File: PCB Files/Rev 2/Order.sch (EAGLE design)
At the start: 188 parts, among them IC1 ATMEGA32A-PU, J1 USB4085-GF-A_REVA, SW1 EC12E_SW, X1 49S/18PF

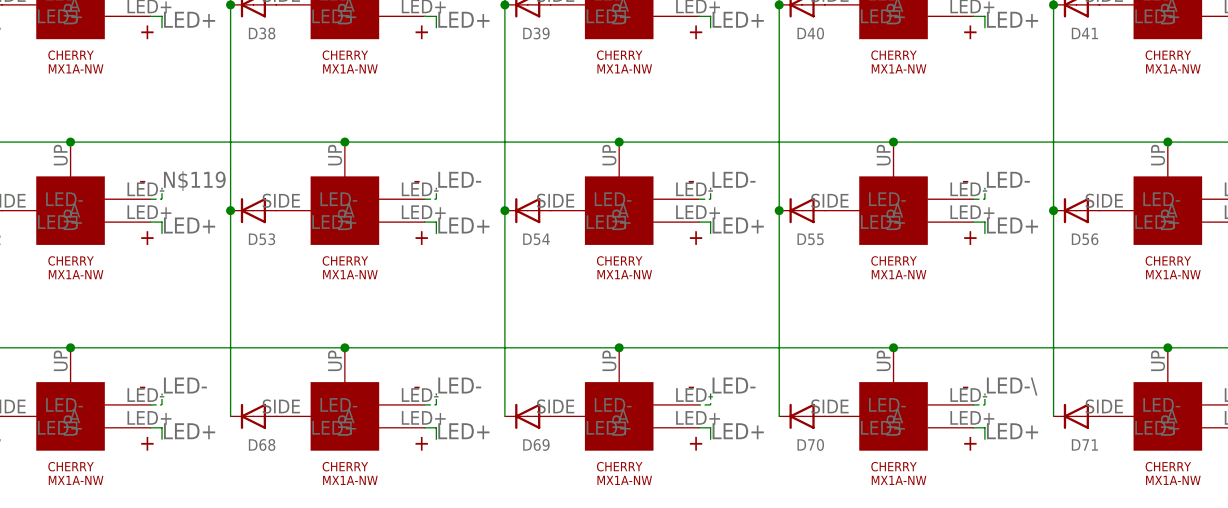
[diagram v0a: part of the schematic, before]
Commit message: now with Traces!
I added the traces to the new, now less stupid PCB.
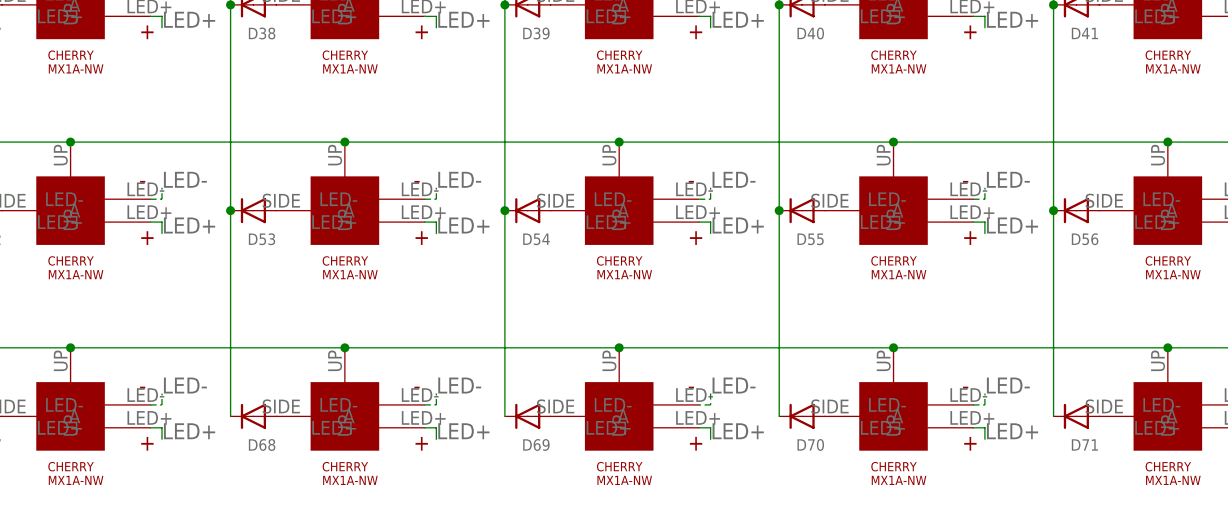
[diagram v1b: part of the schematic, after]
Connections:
- removed net LED-\: U$70.LED-
- removed net N$119: U$52.LED-
- net LED-: now also U$52.LED-, U$70.LED-
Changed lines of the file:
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@@
 <label x="134.62" y="-40.64" size="1.778" layer="95"/>
 </segment>
-</net>
-<net name="N$119" class="0">
 <segment>
 <pinref part="U$52" gate="G$1" pin="LED-"/>
@@
 <label x="195.58" y="-83.82" size="1.778" layer="95"/>
 </segment>
-</net>
-<net name="LED-\" class="0">
 <segment>
 <pinref part="U$70" gate="G$1" pin="LED-"/>
